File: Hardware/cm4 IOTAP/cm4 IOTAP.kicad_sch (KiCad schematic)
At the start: 97 parts, among them IC1 TPS3700-WSON, J1 USB_C_Receptacle_USB2.0, K1 J104D2C3VDC.15S, Q1 AO3400A, U1 MAX15062A, U2 Compute_Module_4_Connectors, U3 PC817, U4 PC817, U5 PC817, U6 PC817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

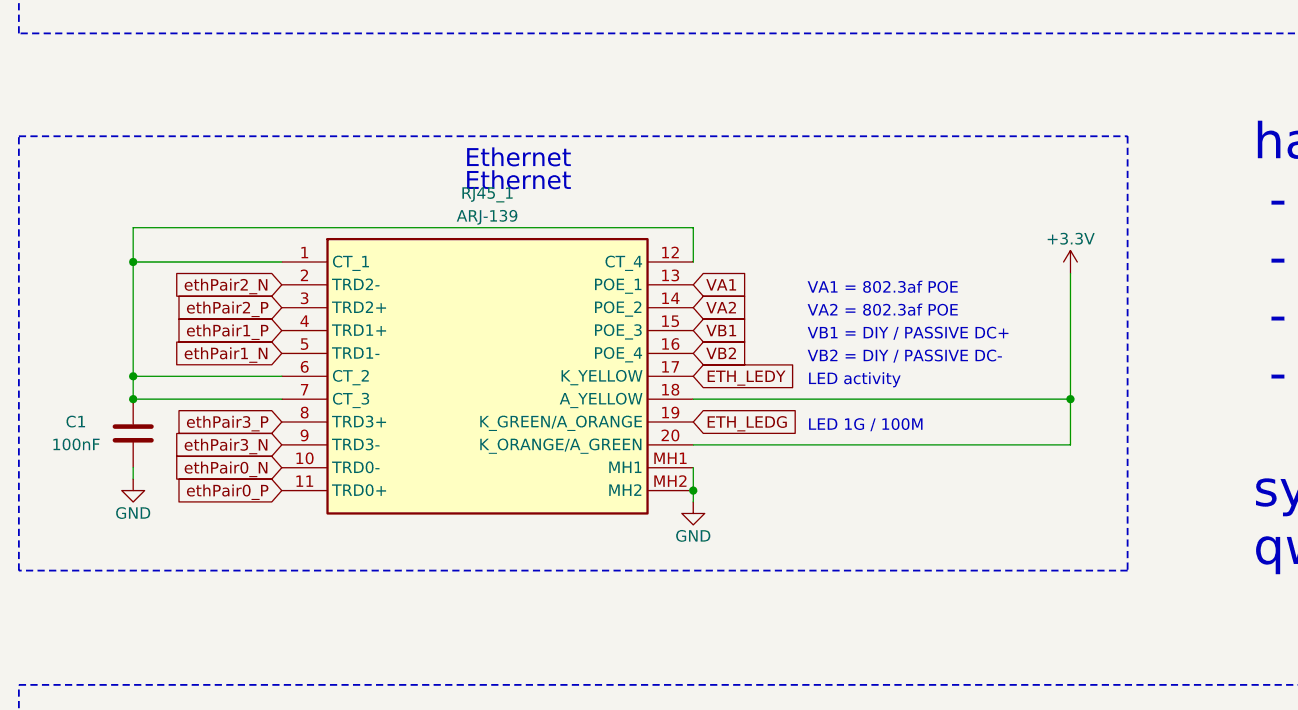
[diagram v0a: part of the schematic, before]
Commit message: add resistors for Ethernet activity lights
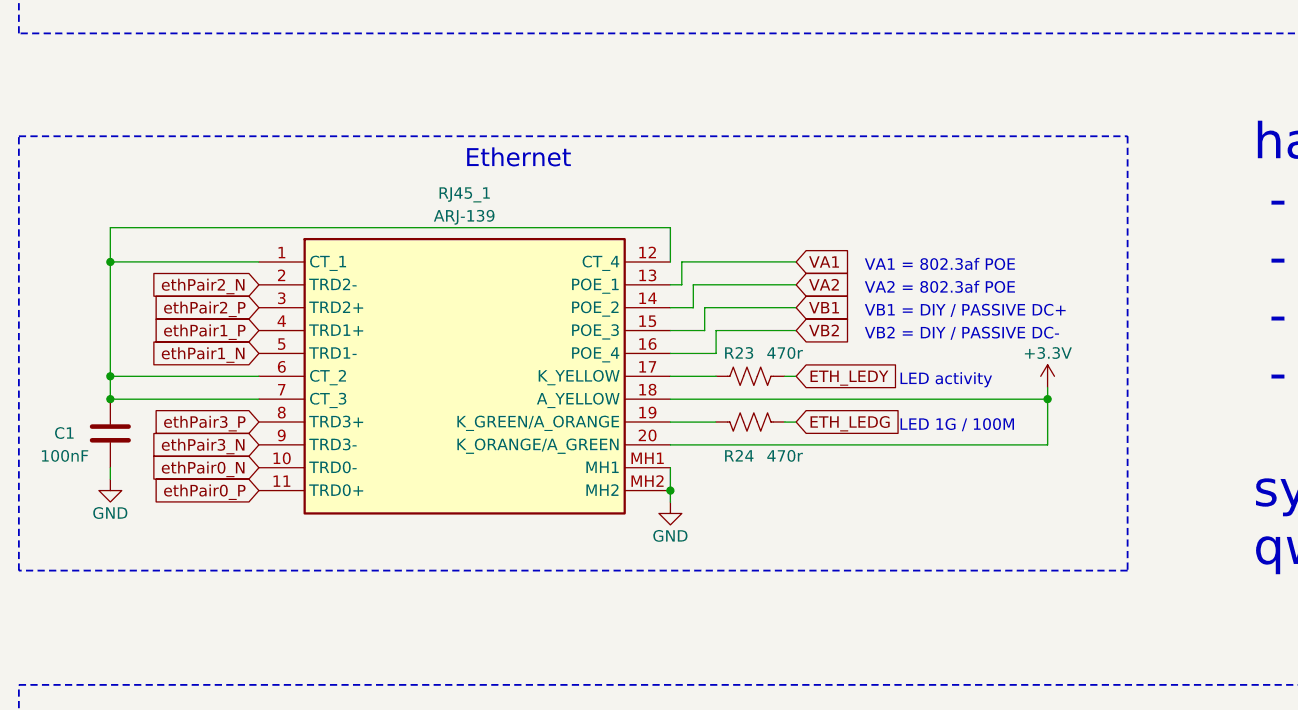
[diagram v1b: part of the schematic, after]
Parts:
- added R23, R24: 470r, Resistor_SMD:R_0603_1608Metric, symbol Device:R_US
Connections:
- net ETH_LEDG: now also R24.2; no longer RJ45_1.19 (K_GREEN/A_ORANGE)
- net ETH_LEDY: now also R23.2; no longer RJ45_1.17 (K_YELLOW)
- new net: R23.1, RJ45_1.17 (K_YELLOW)
- new net: R24.1, RJ45_1.19 (K_GREEN/A_ORANGE)
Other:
- moved on the sheet: C1, RJ45_1
